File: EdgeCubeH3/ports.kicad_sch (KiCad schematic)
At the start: 30 parts, among them J3 USB_A_Stacked, J4 GPDI_A, J5 93626-3006, J6 DBG UART, J7 GPIO, J8 Micro_SD_Card_Det1, Q3 AO3404, U10 USBLC6-4SC6, U11 USBLC6-4SC6, U12 USBLC6-4SC6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

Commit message: Schematic update, PCB started
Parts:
- added C43: 1u, Capacitor_SMD:C_0603_1608Metric, symbol Device:C
- added R43, R44, R45, R46: 3K, Resistor_SMD:R_0603_1608Metric, symbol Device:R
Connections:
- net D1S: now also C43.2
- net GPDI_CLK+: now also U12.6 (I/O4); no longer U12.4 (I/O3)
- net GPDI_CLK-: now also U12.4 (I/O3); no longer U12.6 (I/O4)
- net GPDI_D1+: now also U11.6 (I/O4); no longer U11.4 (I/O3)
- net GPDI_D1-: now also U11.4 (I/O3); no longer U11.6 (I/O4)
- net TWI0_SCK: now also R43.2
- net TWI0_SDA: now also R46.1
- net TWI1_SCK: now also R45.2
- net TWI1_SDA: now also R44.1
- net VBUS: no longer D2.1 (K), J4.18 (+5V)
- net VCC_IO: now also J5.1 (VCC), C43.1, R43.1, R44.2, R45.1, R46.2
- new net: D2.1 (K), J4.18 (+5V)
- no-connect marks 6 -> 5
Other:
- note added: "Current limit 6.4 / 5.6K = 1.14A"
- moved on the sheet: J7

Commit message: PCB design at ~90%
- re-arrangement of components
- connecting dram
- connecting ports
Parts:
- D4: value LED -> PWR
- D5: value LED -> STA
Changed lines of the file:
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@@
 		)
 	)
+	(label "USB2+"
+		(at 53.34 53.34 0)
+		(effects
+			(font
+				(size 1.27 1.27)
+			)
+			(justify left bottom)
+		)
+	)
 	(label "GPDI_D2+"
 		(at 228.6 33.02 180)
@@
 		)
 	)
+	(label "USB2-"
+		(at 53.34 55.88 0)
+		(effects
+			(font
+				(size 1.27 1.27)
+			)
+			(justify left bottom)
+		)
+	)
 	(label "GPDI_SCL"
 		(at 219.71 68.58 180)
@@
 		)
 	)
+	(label "USB1+"
+		(at 53.34 48.26 0)
+		(effects
+			(font
+				(size 1.27 1.27)
+			)
+			(justify left bottom)
+		)
+	)
+	(label "USB1-"
+		(at 53.34 50.8 0)
+		(effects
+			(font
+				(size 1.27 1.27)
+			)
+			(justify left bottom)
+		)
+	)
 	(label "EPHY_TX+"
 		(at 48.26 96.52 180)
@@
 			)
 		)
-		(property "Value" "LED"
+		(property "Value" "STA"
 			(at 76.962 139.192 0)
 			(show_name no)
@@
 			)
 		)
-		(property "Value" "LED"
+		(property "Value" "PWR"
 			(at 76.962 131.318 0)
 			(show_name no)

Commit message: PCB at 98%
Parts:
- J7, R43, R44, R45, R46: now not fitted
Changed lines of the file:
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@@
 		(on_board yes)
 		(in_pos_files yes)
-		(dnp no)
+		(dnp yes)
 		(property "Reference" "R44"
 			(at 190.5 109.22 0)
@@
 		(on_board yes)
 		(in_pos_files yes)
-		(dnp no)
+		(dnp yes)
 		(fields_autoplaced yes)
 		(property "Reference" "J7"
@@
 		(on_board yes)
 		(in_pos_files yes)
-		(dnp no)
+		(dnp yes)
 		(property "Reference" "R43"
 			(at 148.59 92.71 0)
@@
 		(on_board yes)
 		(in_pos_files yes)
-		(dnp no)
+		(dnp yes)
 		(property "Reference" "R45"
 			(at 185.42 111.76 0)
@@
 		(on_board yes)
 		(in_pos_files yes)
-		(dnp no)
+		(dnp yes)
 		(property "Reference" "R46"
 			(at 153.67 90.17 0)

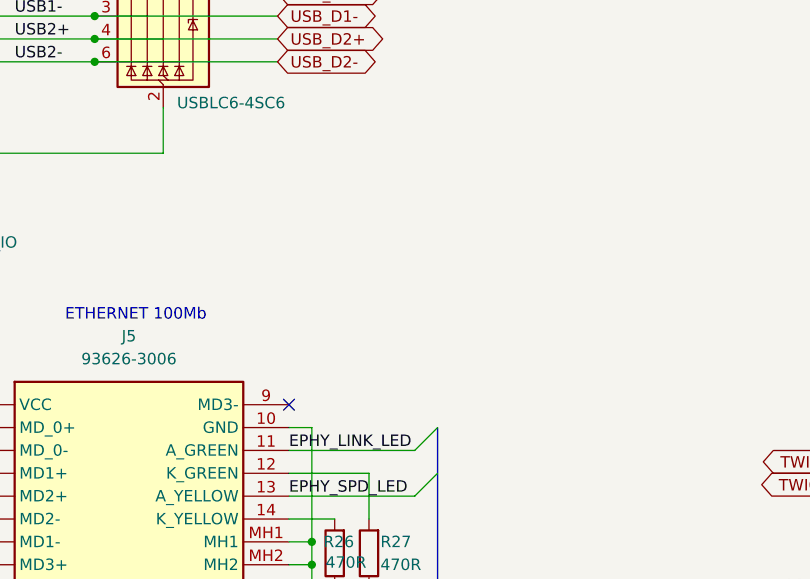
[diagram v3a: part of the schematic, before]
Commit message: Small changes to PCB, updated schematic and readme
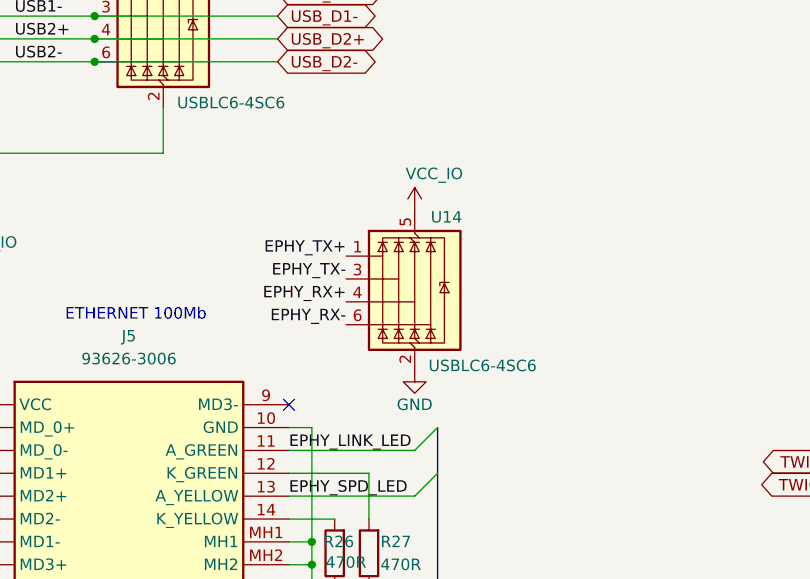
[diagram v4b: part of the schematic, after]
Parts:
- added U14: USBLC6-4SC6, Package_TO_SOT_SMD:SOT-23-6, symbol Power_Protection:USBLC6-4SC6
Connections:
- net D1S: now also U14.2 (GND)
- net EPHY_RX+: now also U14.4 (I/O3)
- net EPHY_RX-: now also U14.6 (I/O4)
- net EPHY_TX+: now also U14.1 (I/O1)
- net EPHY_TX-: now also U14.3 (I/O2)
- net VCC_IO: now also U14.5 (VBUS)
